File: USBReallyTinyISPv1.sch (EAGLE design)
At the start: 20 parts, among them IC1 ATTINY2313, IC2 74AC125D, Q1 12 MHz, X1 miniUSB-B

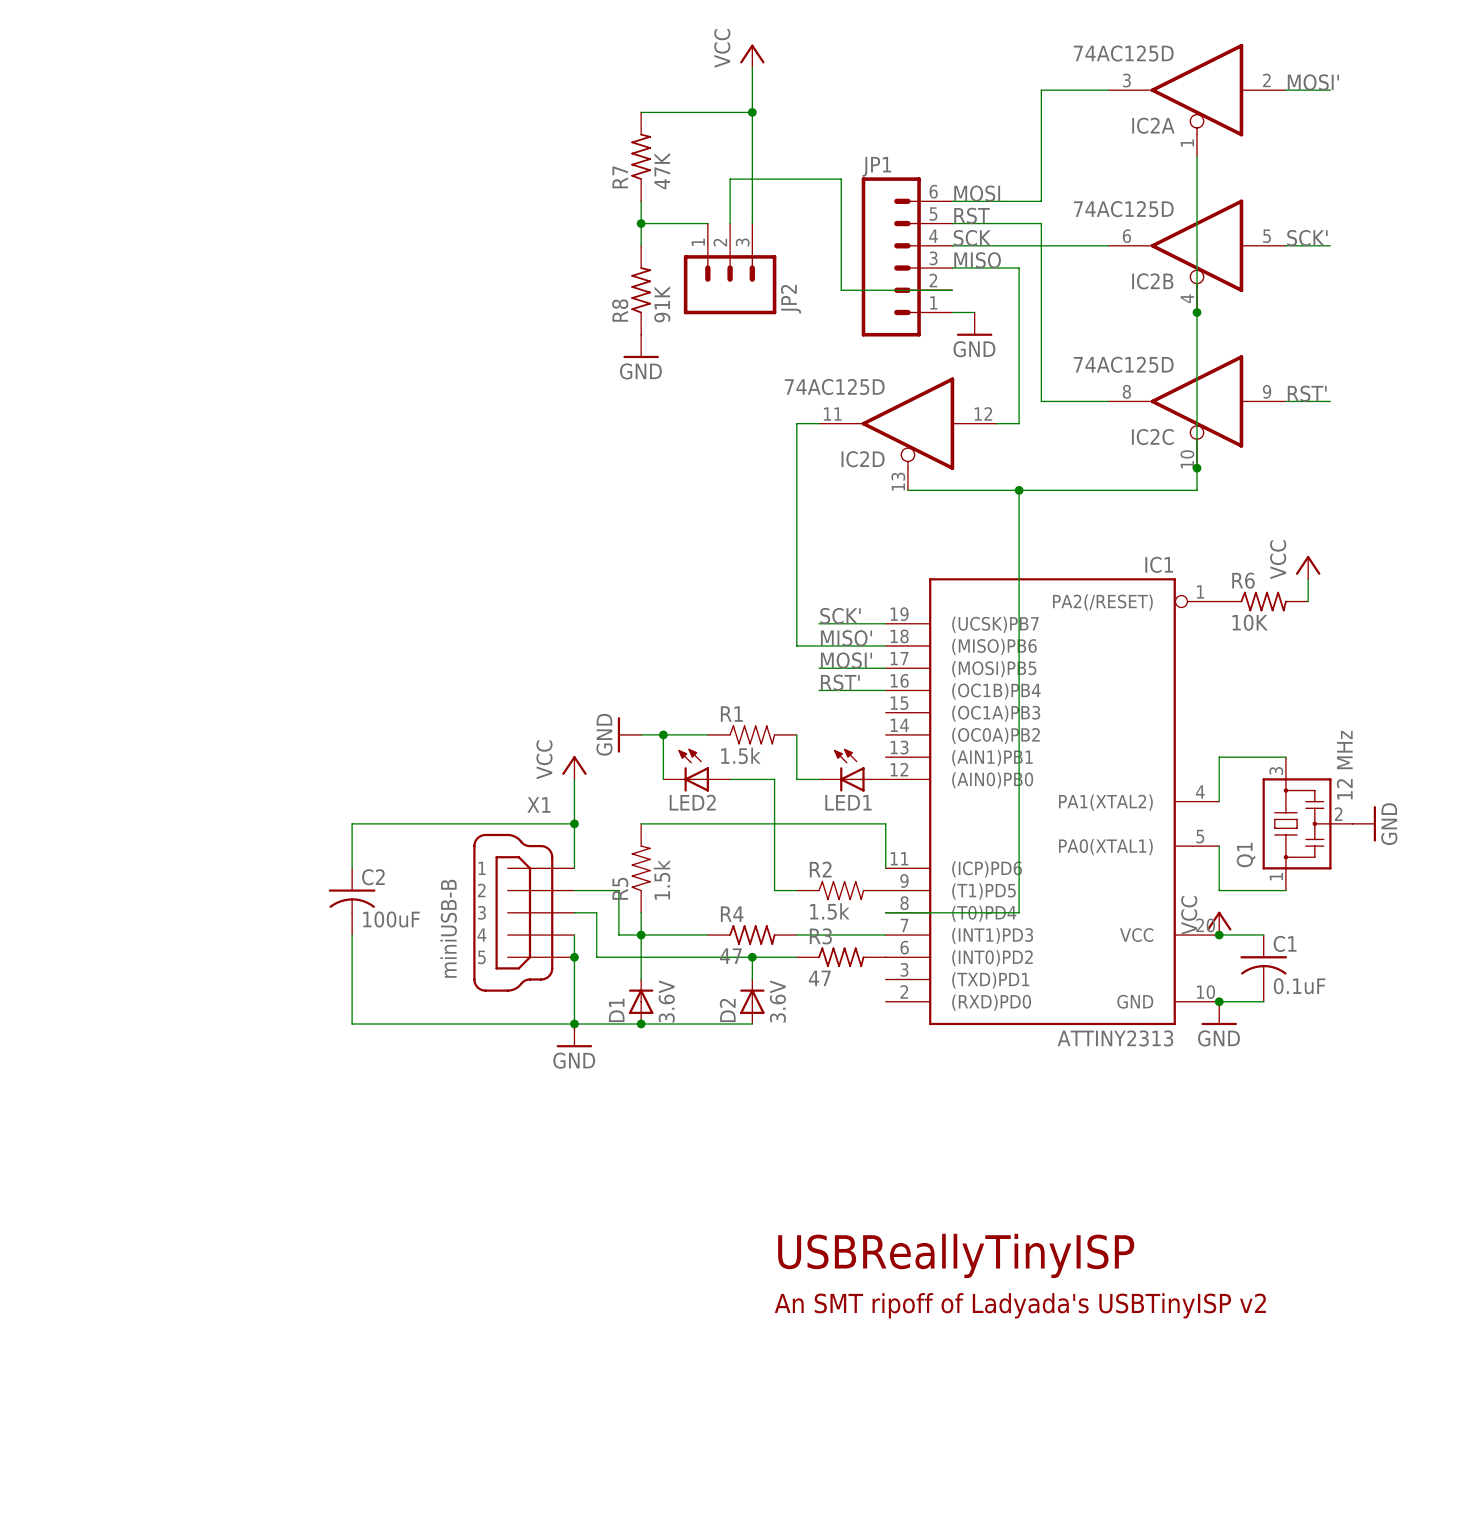
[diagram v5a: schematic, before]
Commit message: Working on the schematic as I start to find flaws in my design
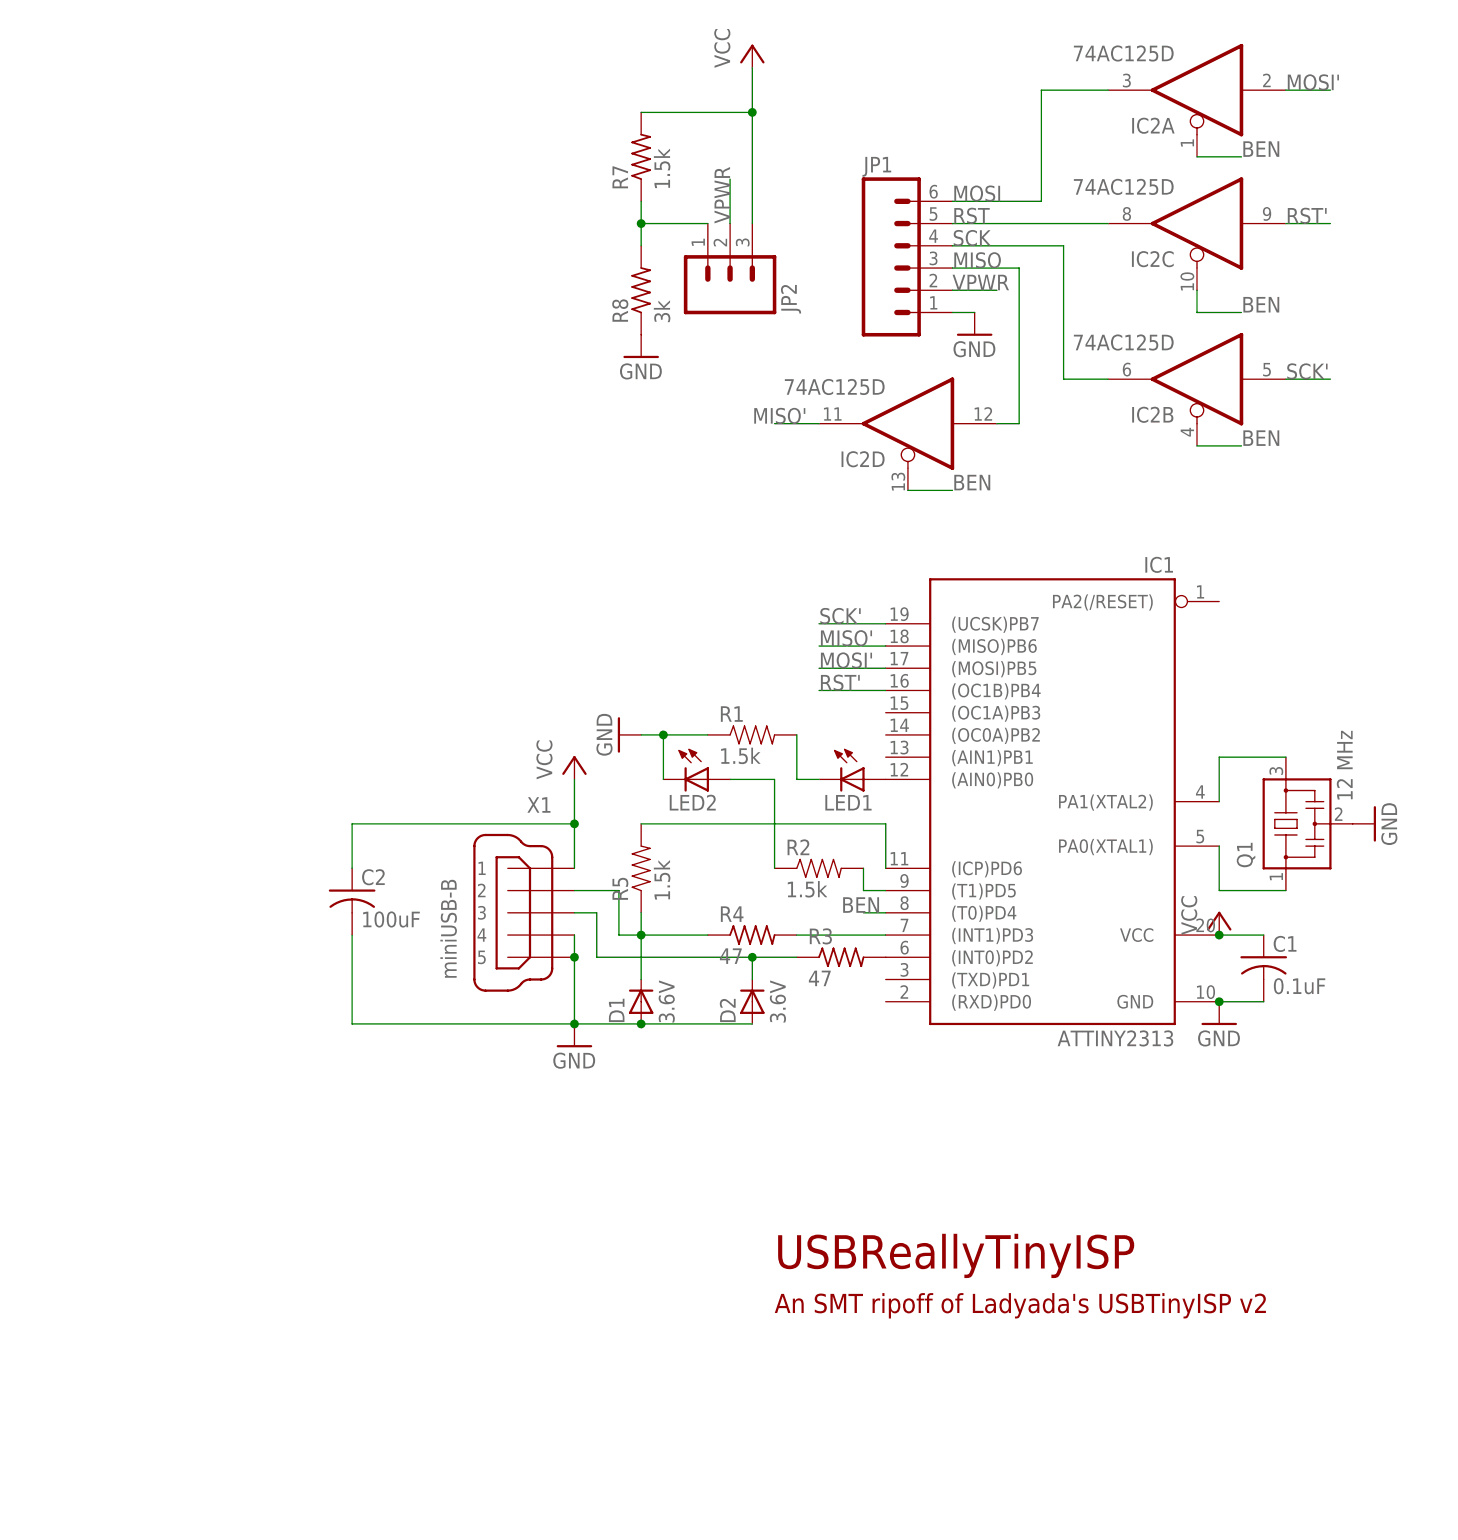
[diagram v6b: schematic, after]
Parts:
- removed R6: 10K, resistor:R-US_R0805
- R7: value 47K -> 1.5k
- R8: value 91K -> 3k
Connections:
- net N$12 renamed BEN
- net N$13 renamed VPWR
- removed net N$4 (its old number): IC1.PA2(/RESET), R6.1
- net RST: no longer IC2C.O
- net VCC: no longer R6.2
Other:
- moved on the sheet: IC2B, IC2C, R2

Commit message: Finally removed that freaking border
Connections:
- net RST: now also IC2C.O
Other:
- note removed: "An SMT ripoff of Ladyada's USBTinyISP v2"
- note removed: "USBReallyTinyISP"
- moved on the sheet: C1, C2, D1, D2, IC1, IC2A, IC2B, IC2C, IC2D, JP1, JP2, LED1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
